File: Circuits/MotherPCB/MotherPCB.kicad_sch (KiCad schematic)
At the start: 0 parts

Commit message: Done for the night
Finished up thermocouple differential communication and every other module apart from PTs and Oil Injector.

Good night.
oh wait
It's 4:00 am.
Good morning
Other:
- added sheet PT1 (PT.kicad_sch)
- added sheet PT2 (PT.kicad_sch)
- added sheet PT3 (PT.kicad_sch)
- added sheet PT4 (PT.kicad_sch)
- added sheet Thermocouple1 (Thermocouple.kicad_sch)
- added sheet Thermocouple2 (Thermocouple.kicad_sch)
- added sheet Thermocouple3 (Thermocouple.kicad_sch)
- added sheet Thermocouple4 (Thermocouple.kicad_sch)
- added sheet Thermocouple5 (Thermocouple.kicad_sch)
- added sheet Thermocouple6 (Thermocouple.kicad_sch)
- added sheet Thermocouple7 (Thermocouple.kicad_sch)
- added sheet Thermocouple8 (Thermocouple.kicad_sch)
- added sheet Thermocouple9 (Thermocouple.kicad_sch)
- sheet FlowSensor ports: added 3V3, GND, PULSE; removed none
- sheet FlowStepper ports: added 3V3, DIR, EN, GND, STP; removed none
- sheet Ignition Coil Trigger ports: added DIR, EN, GND, STP; removed none
- sheet Load Cell ports: added 3V3, GND, MISO, SCK; removed none
- sheet Starter Motor ports: added GND, PWM, VCC; removed none
- sheet Thermocouple ports: added 3.3V, CS, GND, MISO, SCK; removed none
- company: (none) -> Project Arka
- title: (none) -> ECU Motherboard

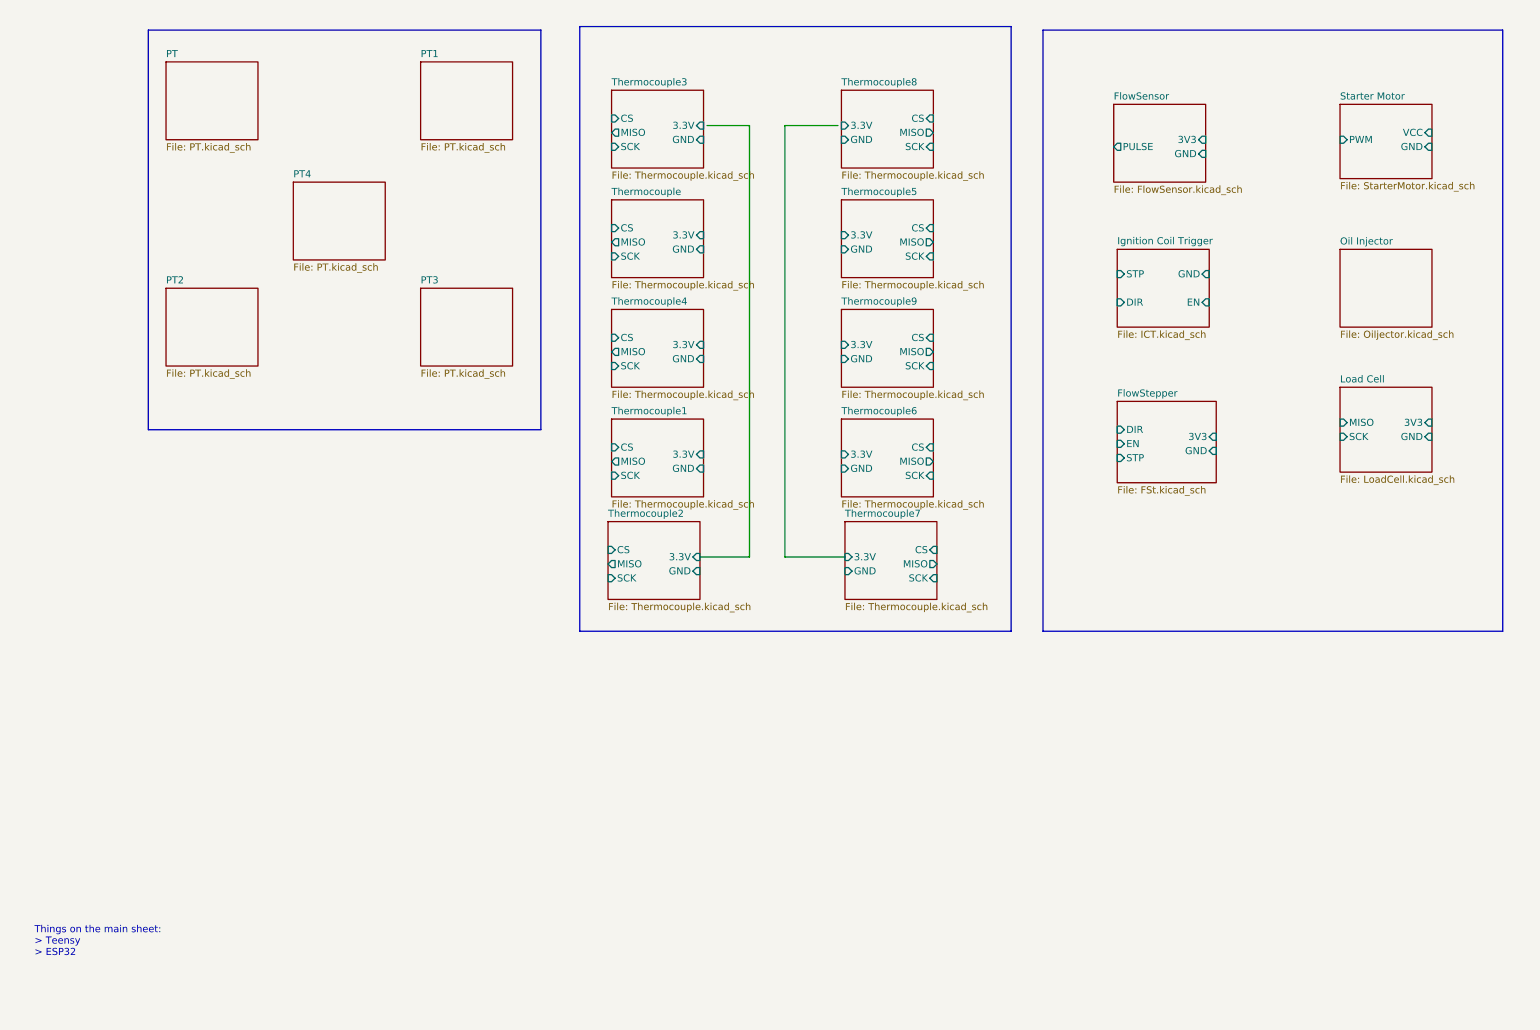
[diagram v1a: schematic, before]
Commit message: Added footprint for ATTiny85 module, added schematic for oil injector circuit
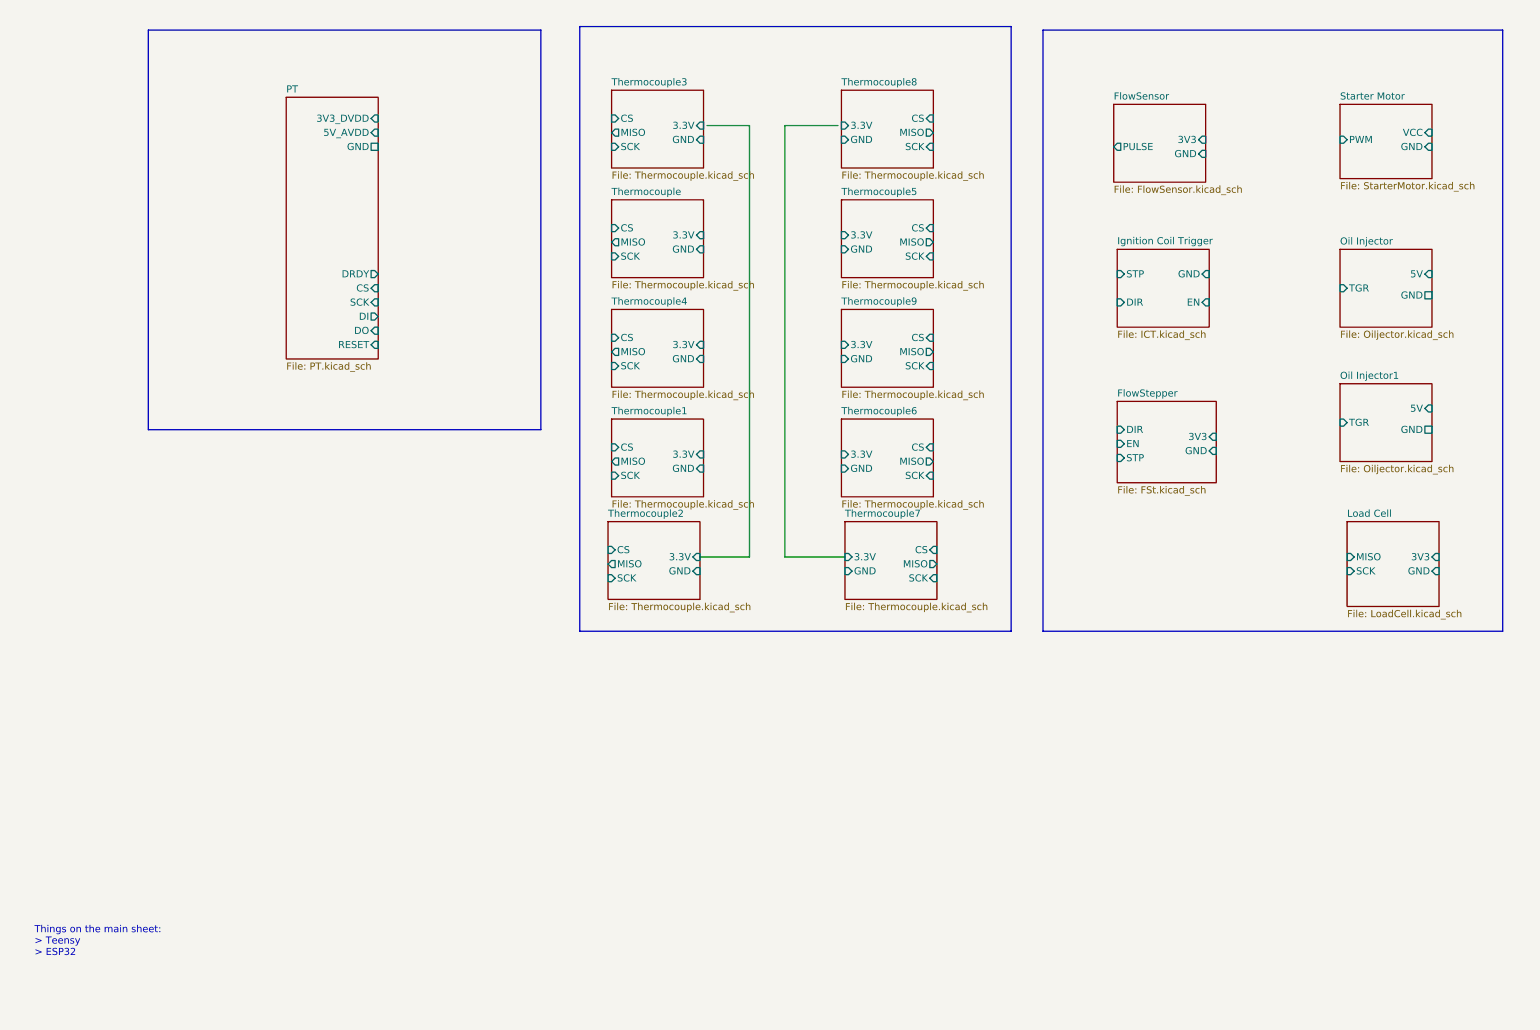
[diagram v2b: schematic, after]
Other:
- removed sheet PT1
- removed sheet PT2
- removed sheet PT3
- removed sheet PT4
- added sheet Oil Injector1 (Oiljector.kicad_sch)
- sheet Oil Injector ports: added 5V, GND, TGR; removed none
- sheet PT ports: added 3V3_DVDD, 5V_AVDD, CS, DI, DO, DRDY, GND, RESET, SCK; removed none

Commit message: Added Teensy and some labels to the schematic
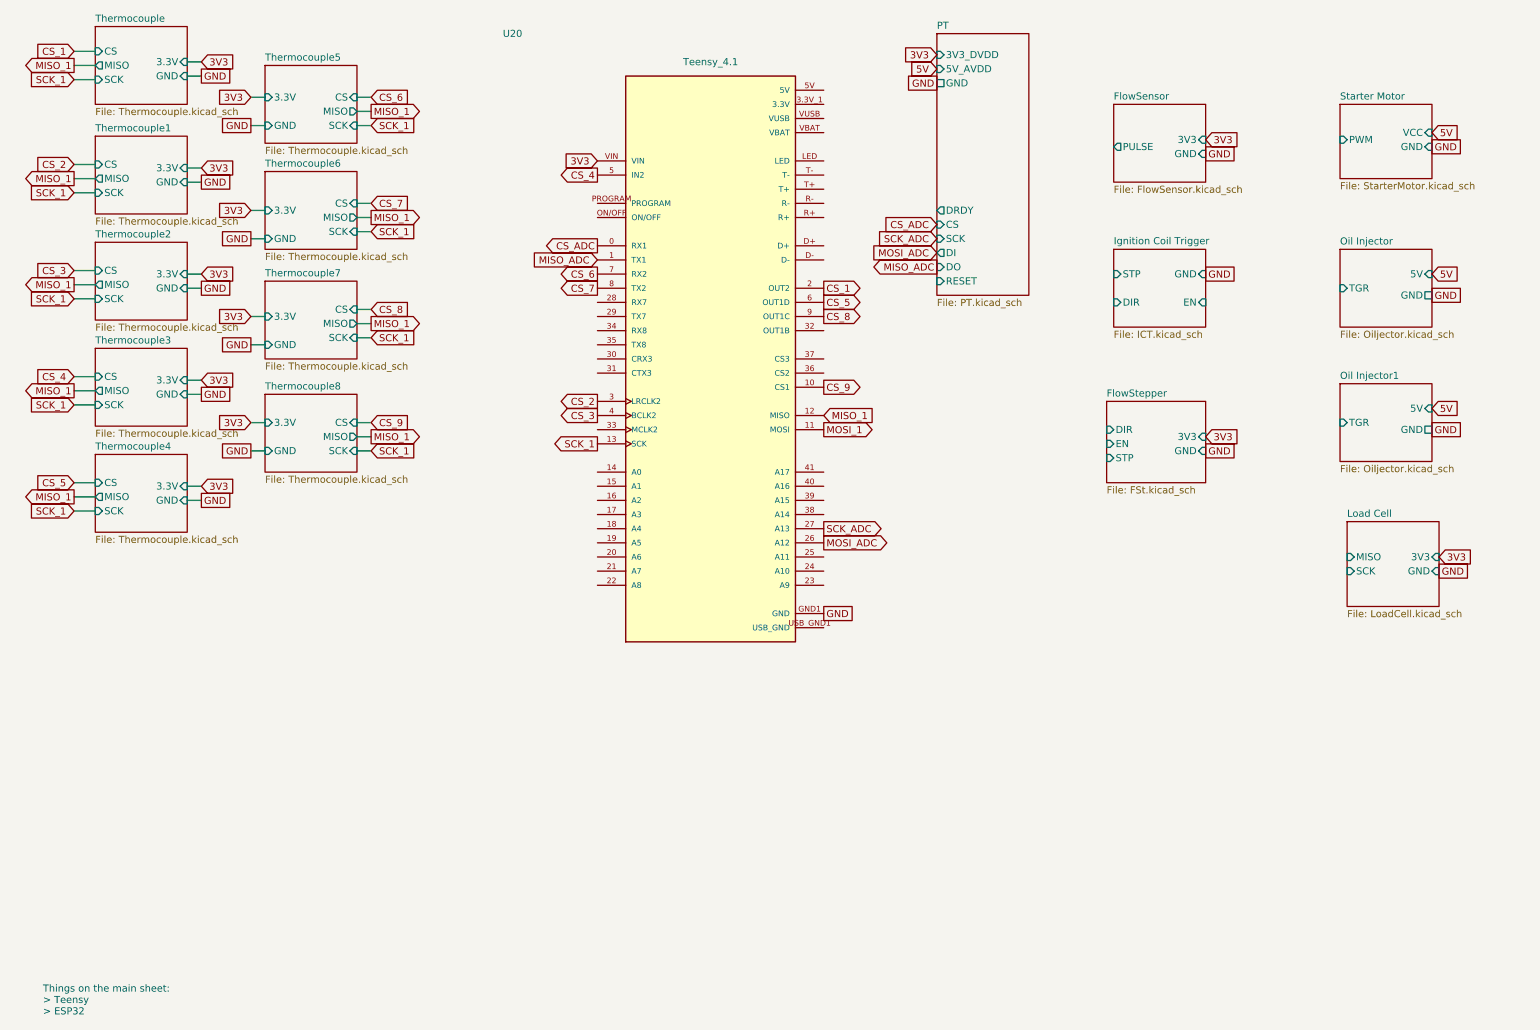
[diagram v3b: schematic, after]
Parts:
- added U20: Teensy_4.1, Additional_Components:Teensy_4.1, symbol Additional_Components:Teensy_4.1
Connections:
- new net 3.3V: U20.3.3V_1 (3.3V), U20.3.3V_2 (3.3V), U20.3.3V_3 (3.3V)
- new net 3V3: U20.VIN
- new net CS_1: U20.2 (OUT2)
- new net CS_2: U20.3 (LRCLK2)
- new net CS_3: U20.4 (BCLK2)
- new net CS_4: U20.5 (IN2)
- new net CS_5: U20.6 (OUT1D)
- new net CS_6: U20.7 (RX2)
- new net CS_7: U20.8 (TX2)
- new net CS_8: U20.9 (OUT1C)
- new net CS_9: U20.10 (CS1)
- new net CS_ADC: U20.0 (RX1)
- new net GND: U20.GND1 (GND), U20.GND2 (GND), U20.GND3 (GND), U20.GND4 (GND), U20.GND5 (GND)
- new net MISO_1: U20.12 (MISO)
- new net MISO_ADC: U20.1 (TX1)
- new net MOSI_1: U20.11 (MOSI)
- new net MOSI_ADC: U20.26 (A12)
- new net SCK_1: U20.13 (SCK)
- new net SCK_ADC: U20.27 (A13)
- new net USB_GND: U20.USB_GND1 (USB_GND), U20.USB_GND2 (USB_GND)
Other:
- removed sheet Thermocouple9

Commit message: Schematic Finished
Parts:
- added U18: ESP32-DEVKITC-32E, ESP32-DEVKITC-32E:MODULE_ESP32-DEVKITC-32E, symbol Additional_Components:ESP32-DEVKITC-32E
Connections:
- net GND: now also U18.J3_1 (GND_J3_1)
- net STARTER_PWM: now reaches U20.14 (A0)
- net SDA_IC: now reaches U20.18 (A4)
- net SDA_IC: now also U18.J3_6 (IO21)
- net SCL_IC: now reaches U20.19 (A5)
- net SCL_IC: now also U18.J3_3 (IO22)
- net STEPPER_EN: now reaches U20.21 (A7)
- net STEPPER_DIR: now reaches U20.22 (A8)
- net STEPPER_PWM: now reaches U20.23 (A9)
- net OI_TGR: now reaches U20.24 (A10)
- net IGNITION_TGR: now reaches U20.25 (A11)
- net T_PULSE: now reaches U20.38 (A14)
- net LC_SCK: now reaches U20.39 (A15)
- net LC_MISO: now reaches U20.40 (A16)
- net FLOW_PULSE: now reaches U20.41 (A17)
- net 3V3 renamed +5VA
- new net +3V3: U18.J2_1 (3V3)
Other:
- added sheet Tachometer (Tachometer.kicad_sch)
- sheet Ignition Coil Trigger ports: added 5V, TGR; removed DIR, EN, STP

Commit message: Fixed some broken footprints
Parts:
- U18: footprint ESP32-DEVKITC-32E:MODULE_ESP32-DEVKITC-32E -> Additional_Components:MODULE_ESP32-DEVKITC-32E
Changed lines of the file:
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@@
 			)
 		)
-		(property "Footprint" "ESP32-DEVKITC-32E:MODULE_ESP32-DEVKITC-32E"
+		(property "Footprint" "Additional_Components:MODULE_ESP32-DEVKITC-32E"
 			(at 210.82 135.89 0)
 			(effects

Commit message: pcb completed with a clean DRC
first one it is let us pray it works
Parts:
- added R11: 10k, Resistor_THT:R_Axial_DIN0207_L6.3mm_D2.5mm_P7.62mm_Horizontal, symbol Device:R
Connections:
- net +3V3: now also R11.1
- net MISO_1: now also R11.2
- no-connect marks 0 -> 61
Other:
- added sheet Power Supply (pSupply.kicad_sch)

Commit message: PCB v2 um
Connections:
- net +5VA: now also U18.J2_19 (EXT_5V)
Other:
- sheet FlowSensor ports: added 5V; removed none
- sheet Tachometer ports: added SIG; removed 3V3, PULSE
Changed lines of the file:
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@@
 	)
 	(no_connect
+		(at 179.07 49.53)
+	)
+	(no_connect
 		(at 231.14 120.65)
 	)
@@
 	)
 	(no_connect
-		(at 190.5 158.75)
-	)
-	(no_connect
 		(at 190.5 148.59)
 	)
@@
 	(wire
 		(pts
+			(xy 182.88 154.94) (xy 182.88 158.75)
+		)
+		(stroke
+			(width 0)
+			(type default)
+		)
+	)
+	(wire
+		(pts
 			(xy 44.45 101.6) (xy 46.99 101.6)
 		)
@@
 	(wire
 		(pts
+			(xy 182.88 158.75) (xy 190.5 158.75)
+		)
+		(stroke
+			(width 0)
+			(type default)
+		)
+	)
+	(wire
+		(pts
 			(xy 55.88 34.29) (xy 58.42 34.29)
 		)
@@
 		)
 	)
+	(global_label "5V"
+		(shape input)
+		(at 227.33 34.29 0)
+		(fields_autoplaced yes)
+		(effects
+			(font
+				(size 1.27 1.27)
+			)
+			(justify left)
+		)
+		(property "Intersheetrefs" "${INTERSHEET_REFS}"
+			(at 232.6133 34.29 0)
+			(effects
+				(font
+					(size 1.27 1.27)
+				)
+				(justify left)
+				(hide yes)
+			)
+		)
+	)
 	(global_label "SCK_1"
 		(shape input)
@@
 	(global_label "T_PULSE"
 		(shape output)
-		(at 252.73 140.97 180)
+		(at 252.73 144.78 180)
 		(fields_autoplaced yes)
 		(effects
@@
 		)
 		(property "Intersheetrefs" "${INTERSHEET_REFS}"
-			(at 241.8225 140.97 0)
+			(at 241.8225 144.78 0)
 			(effects
 				(font
@@
 		)
 	)
-	(global_label "3V3"
-		(shape input)
-		(at 269.24 143.51 0)
-		(fields_autoplaced yes)
-		(effects
-			(font
-				(size 1.27 1.27)
-			)
-			(justify left)
-		)
-		(property "Intersheetrefs" "${INTERSHEET_REFS}"
-			(at 275.7328 143.51 0)
-			(effects
-				(font
-					(size 1.27 1.27)
-				)
-				(justify left)
-				(hide yes)
-			)
-		)
-	)
 	(global_label "SCK_1"
 		(shape input)
@@
 	)
 	(symbol
+		(lib_id "power:+5VA")
+		(at 182.88 154.94 0)
+		(unit 1)
+		(exclude_from_sim no)
+		(in_bom yes)
+		(on_board yes)
+		(dnp no)
+		(fields_autoplaced yes)
+		(property "Reference" "#PWR07"
+			(at 182.88 158.75 0)
+			(effects
+				(font
+					(size 1.27 1.27)
+				)
+				(hide yes)
+			)
+		)
+		(property "Value" "+5VA"
+			(at 182.88 149.86 0)
+			(effects
+				(font
+					(size 1.27 1.27)
+				)
+			)
+		)
+		(property "Footprint" ""
+			(at 182.88 154.94 0)
+			(effects
+				(font
+					(size 1.27 1.27)
+				)
+				(hide yes)
+			)
+		)
+		(property "Datasheet" ""
+			(at 182.88 154.94 0)
+			(effects
+				(font
+					(size 1.27 1.27)
+				)
+				(hide yes)
+			)
+		)
+		(property "Description" "Power symbol creates a global label with name \"+5VA\""
+			(at 182.88 154.94 0)
+			(effects
+				(font
+					(size 1.27 1.27)
+				)
+				(hide yes)
+			)
+		)
+		(pin "1"
+		)
+		(instances
+			(project "MotherPCB"
+				(path "/ea485091-218e-4ddf-97d6-ebaac999a2f0"
+					(reference "#PWR07")
+					(unit 1)
+				)
+			)
+		)
+	)
+	(symbol
 		(lib_id "Device:R")
 		(at 172.72 82.55 0)
@@
 			)
 		)
+		(pin "5V" input
+			(at 227.33 34.29 0)
+			(effects
+				(font
+					(size 1.27 1.27)
+				)
+				(justify right)
+			)
+		)
 		(instances
 			(project "MotherPCB"
@@
 			)
 		)
-		(pin "PULSE" output
-			(at 252.73 140.97 180)
-			(effects
-				(font
-					(size 1.27 1.27)
-				)
-				(justify left)
-			)
-		)
 		(pin "5V" input
 			(at 269.24 140.97 0)
@@
 			)
 		)
-		(pin "3V3" input
-			(at 269.24 143.51 0)
+		(pin "SIG" output
+			(at 252.73 144.78 180)
 			(effects
 				(font
 					(size 1.27 1.27)
 				)
-				(justify right)
+				(justify left)
 			)
 		)
